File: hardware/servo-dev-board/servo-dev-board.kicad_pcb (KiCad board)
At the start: 4 copper layers, 51.5 x 26.5 mm, 39 parts, among them J1 USB_B_Micro, J2 Conn_01x05_MountingPin, J3 Conn_01x04_MountingPin, J4 Conn_01x04_MountingPin, J5 Conn_02x05_Odd_Even, SW1 SW_Push, SW2 SW_Push, U1 DRV8231ADSGR, U2 SSP7615-33DFR, U3 STM32F301K8Ux, Y1 16MHz 9pF

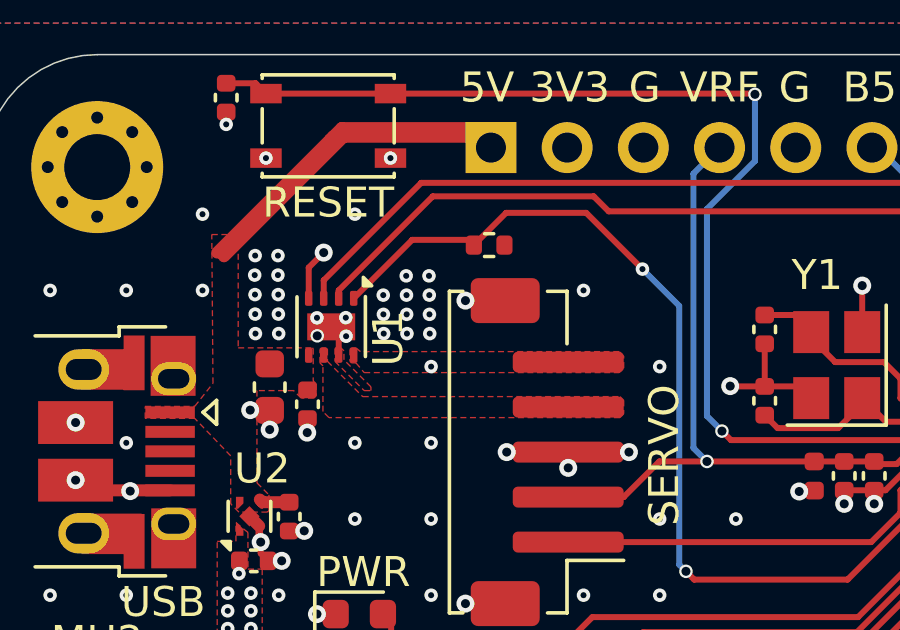
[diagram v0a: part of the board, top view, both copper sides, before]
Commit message: Fixed error in PCB. Lowered isense resistor to 1.5k Ohm to increase max servo current to 1.5A
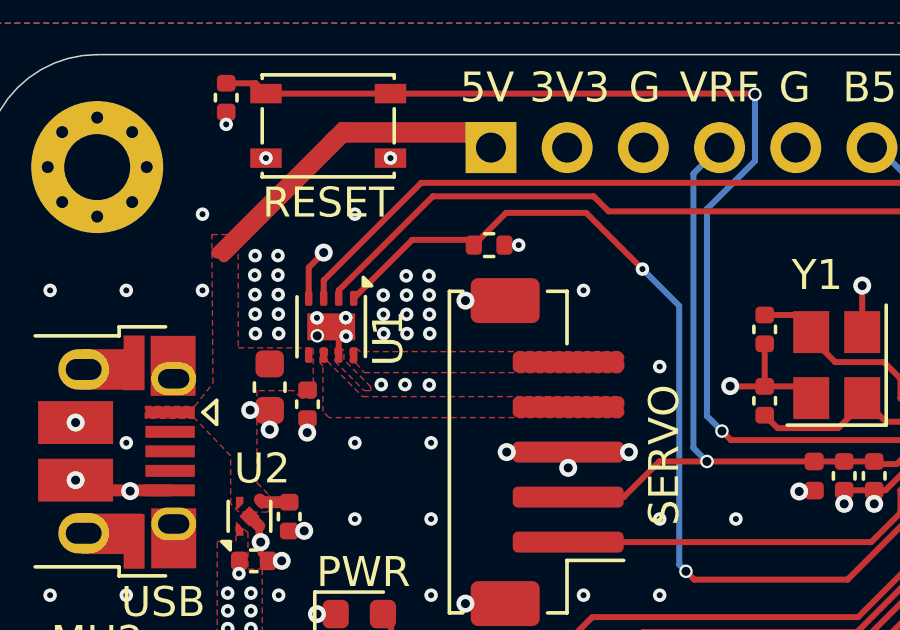
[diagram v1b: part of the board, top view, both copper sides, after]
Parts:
- R7: value 2K2 -> 1K5
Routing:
- net GND: vias 114 -> 117
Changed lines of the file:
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@@
 			)
 		)
-		(property "Value" "2K2"
+		(property "Value" "1K5"
 			(at 0 1.17 0)
 			(layer "F.Fab")
@@
 			)
 		)
-		(property "LCSC" "C25768"
+		(property "LCSC" "C25867"
 			(at 0 0 0)
 			(layer "F.SilkS")
@@
 		(sheetname "Root")
 		(sheetfile "servo-dev-board.kicad_sch")
-		(attr smd)
+		(attr through_hole)
 		(fp_line
 			(start -3.875 2.735)
@@
 			)
 		)
+		(property "LCSC" "C3011523"
+			(at 0 0 90)
+			(unlocked yes)
+			(layer "F.Fab")
+			(hide yes)
+			(effects
+				(font
+					(size 1 1)
+					(thickness 0.15)
+				)
+			)
+		)
 		(sheetname "Root")
 		(sheetfile "servo-dev-board.kicad_sch")
@@
 			)
 		)
+		(property "LCSC" "C5139865"
+			(at 0 0 -90)
+			(unlocked yes)
+			(layer "F.Fab")
+			(hide yes)
+			(effects
+				(font
+					(size 1 1)
+					(thickness 0.15)
+				)
+			)
+		)
 		(sheetname "Root")
 		(sheetfile "servo-dev-board.kicad_sch")
@@
 	)
 	(via
+		(at 132.05 94.1)
+		(size 0.45)
+		(drill 0.2)
+		(layers "F.Cu" "B.Cu")
+		(free yes)
+		(net 2)
+	)
+	(via
 		(at 136.75 105.77)
 		(size 0.45)
@@
 	)
 	(via
-		(at 129.13 98.15)
+		(at 129.07 98.76)
 		(size 0.45)
 		(drill 0.2)
@@
 	)
 	(via
+		(at 128.26 98.75)
+		(size 0.45)
+		(drill 0.2)
+		(layers "F.Cu" "B.Cu")
+		(free yes)
+		(net 2)
+	)
+	(via
 		(at 121.51 93.07)
 		(size 0.45)
@@
 		(net 2)
 	)
+	(via
+		(at 127.47 98.75)
+		(size 0.45)
+		(drill 0.2)
+		(layers "F.Cu" "B.Cu")
+		(free yes)
+		(net 2)
+	)

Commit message: added version, board, author info
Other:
- board text added: "SMART SERVO BOARD MCU: STM32F301 Version: 1.0.0 Designed By: Aaron Qian"
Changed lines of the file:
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@@
+		)
+	)
+	(gr_text "SMART SERVO BOARD\nMCU: STM32F301\nVersion:  1.0.0\nDesigned By: Aaron Qian"
+		(at 129.47 96.55 180)
+		(layer "B.SilkS")
+		(effects
+			(font
+				(size 1.5 1.5)
+				(thickness 0.1)
+			)
+			(justify left bottom mirror)
 		)
 	)
